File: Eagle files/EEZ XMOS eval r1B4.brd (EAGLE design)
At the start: 100 x 85 mm, 227 parts, among them IC1 TPS61169DCKR, IC10 IS42S16400J, IC11 SN74CBTLV3257, IC12 SN74LVC1G02DBVR, IC13 AT25SF041-SSHDT, IC14 SN74CBTLV3257, IC15 TPS2051BDBVR, IC16 TPD2E001DZDR, IC17 TPS561208DDCR, IC18 XE216-512-TQ128-C20, IC19 TPD4E001DRLR, IC2 TPS561208DDCR, IC20 TPD4E001DRLR, IC21 74LVC1G07SE-7, IC22 74LVC1G07SE-7, IC23 TPA6205A1DGN, IC24 DP83848CVV/NOPB, IC25 M95256-WMN6P, IC26 74VHC595MTC, IC27 PCA21125T/Q900/1,1, IC28 MCP23S17-E/SS, IC3 74VHC595MTC, IC4 TPS561208DDCR, IC5 74VHC595MTC, IC6 TPS3808G33DBVR, IC7 AR1021-I/SS, IC8 TPS3808G09DBVR, IC9 74AUP1G74DC.125, J1 678038020, J2 5033981892, Q1 IRLML2246TRPBF, SW1 1301.9316, X1 FC68149, X2 SSW-105-02-S-D, X3 TSW-104-02-S-D_NN, X4 TSW-103-07-F-D, X5 ZL231-20KG, X6 22-23-2021, X7 LMJTAB881243M-L, X8 SSW-107-02-S-D, X9 PCA-6G-20-HL-3 or 52746-2071, Y1 XTAL016178- 85SMX

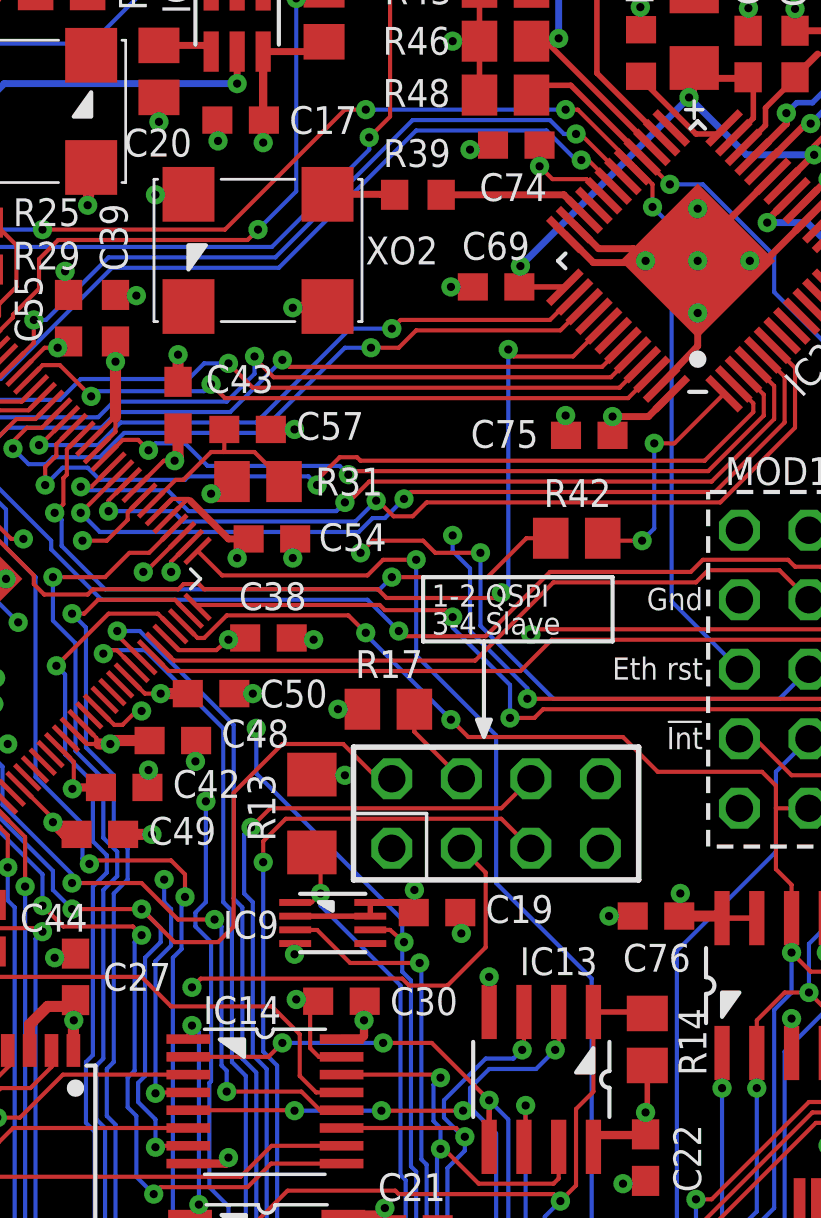
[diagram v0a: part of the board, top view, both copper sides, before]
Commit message: pin swap on X3
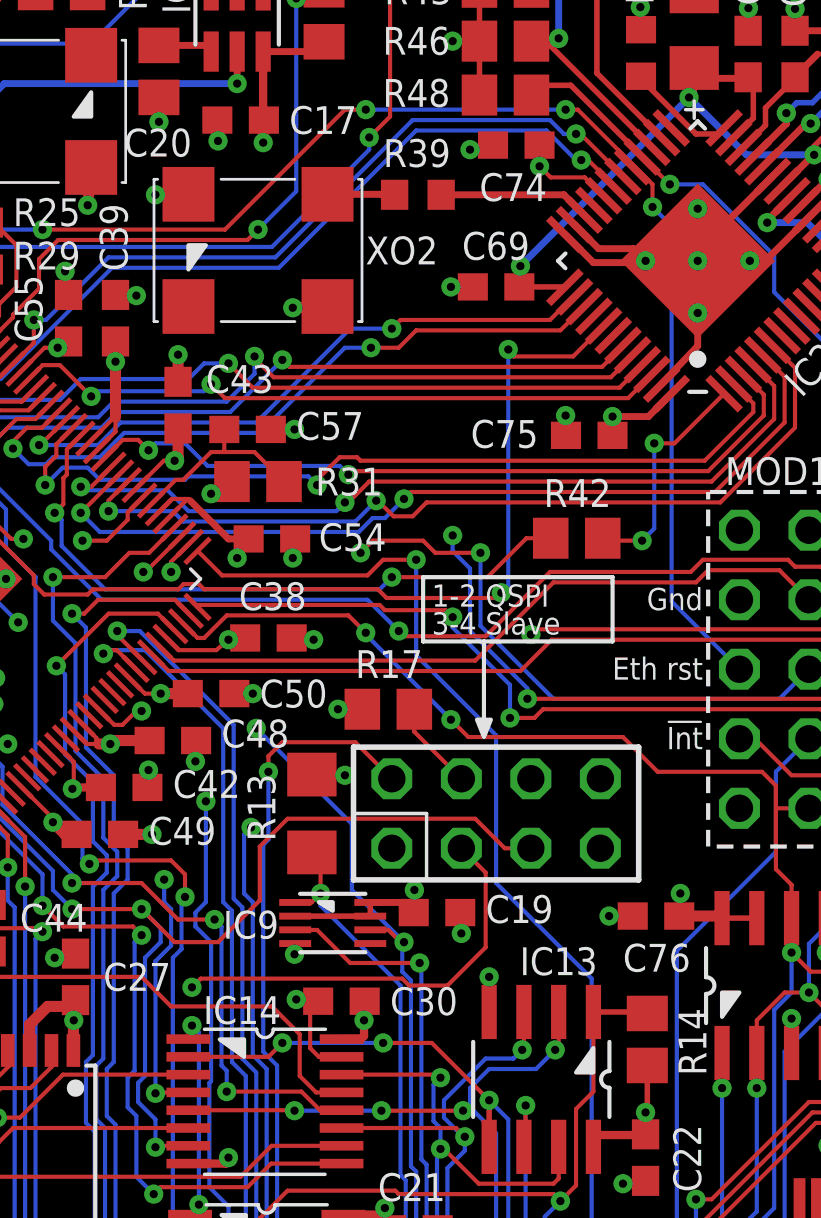
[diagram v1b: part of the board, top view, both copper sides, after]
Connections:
- net LATCH_IN: now also X3.2; no longer X3.5
- net X0D05/QS_D1: now also X3.5; no longer X3.2
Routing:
- net X0D05/QS_D1: track 51.6 -> 53.7 mm
- net LATCH_IN: track 30.9 -> 28.8 mm
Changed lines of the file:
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@@
 <layer number="27" name="tValues" color="12" fill="1" visible="no" active="yes"/>
 <layer number="28" name="bValues" color="11" fill="1" visible="no" active="yes"/>
-<layer number="29" name="tStop" color="7" fill="1" visible="no" active="yes"/>
+<layer number="29" name="tStop" color="7" fill="1" visible="yes" active="yes"/>
 <layer number="30" name="bStop" color="7" fill="1" visible="no" active="yes"/>
 <layer number="31" name="tCream" color="7" fill="4" visible="no" active="yes"/>
@@
 <wire x1="69.4055" y1="71.462" x2="69.4055" y2="72.4154" width="0.254" layer="1"/>
 <wire x1="60.949065625" y1="62.005771875" x2="60.930228125" y2="62.005771875" width="0.2032" layer="1"/>
-<wire x1="60.930228125" y1="62.005771875" x2="60.325" y2="62.611" width="0.1524" layer="1"/>
-<wire x1="60.325" y1="62.611" x2="59.0804" y2="62.611" width="0.1524" layer="1"/>
-<wire x1="59.0804" y1="62.611" x2="58.6105" y2="63.0809" width="0.1524" layer="1"/>
 <wire x1="42.155628125" y1="52.9911" x2="43.076028125" y2="53.9115" width="0.1524" layer="1"/>
 <wire x1="43.1165" y1="55.9435" x2="43.1165" y2="56.681" width="0.4064" layer="1"/>
@@
 <wire x1="29.637284375" y1="53.2765" x2="29.0195" y2="53.2765" width="0.1524" layer="1"/>
 <wire x1="29.0195" y1="53.2765" x2="28.6385" y2="52.8955" width="0.1524" layer="1"/>
+<wire x1="60.930228125" y1="62.005771875" x2="60.2615" y2="62.6745" width="0.1524" layer="1"/>
+<wire x1="60.2615" y1="62.6745" x2="59.0169" y2="62.6745" width="0.1524" layer="1"/>
+<wire x1="59.0169" y1="62.6745" x2="58.6105" y2="63.0809" width="0.1524" layer="1"/>
 </signal>
 <signal name="N$28">
@@
 <wire x1="50.546" y1="12.065" x2="50.8" y2="12.319" width="0.1524" layer="16"/>
 <wire x1="54.102" y1="18.8595" x2="54.102" y2="19.812" width="0.1524" layer="16"/>
-<wire x1="52.4256" y1="35.183" x2="53.1455" y2="35.183" width="0.1524" layer="1"/>
-<wire x1="53.1455" y1="35.183" x2="53.6575" y2="34.7345" width="0.1524" layer="1"/>
 <wire x1="54.102" y1="19.812" x2="54.102" y2="26.3525" width="0.1524" layer="16"/>
 <wire x1="54.102" y1="19.812" x2="54.1655" y2="19.812" width="0.1524" layer="1"/>
@@
 <wire x1="53.9115" y1="33.3375" x2="53.594" y2="33.655" width="0.1524" layer="16"/>
 <wire x1="53.594" y1="33.655" x2="53.594" y2="34.671" width="0.1524" layer="16"/>
-<wire x1="53.594" y1="34.671" x2="53.6575" y2="34.7345" width="0.1524" layer="16"/>
 <wire x1="33.7185" y1="53.5305" x2="24.3205" y2="53.5305" width="0.1524" layer="16"/>
 <wire x1="24.3205" y1="53.5305" x2="23.5585" y2="52.7685" width="0.1524" layer="16"/>
@@
 <wire x1="35.687" y1="50.292" x2="39.5605" y2="46.4185" width="0.1524" layer="16"/>
 <via x="48.26" y="42.545" extent="1-16" drill="0.3" shape="octagon"/>
-<wire x1="48.26" y1="42.545" x2="48.26" y2="40.894" width="0.1524" layer="16"/>
-<wire x1="48.26" y1="40.894" x2="53.594" y2="35.56" width="0.1524" layer="16"/>
-<wire x1="53.594" y1="35.56" x2="53.594" y2="34.798" width="0.1524" layer="16"/>
-<wire x1="53.594" y1="34.798" x2="53.6575" y2="34.7345" width="0.1524" layer="16"/>
 <wire x1="23.495" y1="52.7685" x2="18.669" y2="47.9425" width="0.1524" layer="1"/>
 <wire x1="18.669" y1="47.9425" x2="15.243" y2="47.9425" width="0.1524" layer="1"/>
@@
 <wire x1="39.37" y1="57.559378125" x2="39.369996875" y2="57.559378125" width="0.1524" layer="1"/>
 <wire x1="39.369996875" y1="57.559378125" x2="38.478675" y2="56.66805625" width="0.1524" layer="1"/>
+<wire x1="48.26" y1="42.545" x2="51.7525" y2="39.0525" width="0.1524" layer="16"/>
+<wire x1="51.7525" y1="39.0525" x2="51.7525" y2="36.6395" width="0.1524" layer="16"/>
+<wire x1="53.594" y1="34.671" x2="53.6575" y2="34.7345" width="0.1524" layer="16"/>
+<wire x1="52.4256" y1="35.183" x2="53.082" y2="35.183" width="0.1524" layer="1"/>
+<wire x1="53.6575" y1="34.7345" x2="53.5305" y2="34.7345" width="0.1524" layer="1"/>
+<wire x1="53.5305" y1="34.7345" x2="53.082" y2="35.183" width="0.1524" layer="1"/>
+<wire x1="51.7525" y1="36.6395" x2="53.6575" y2="34.7345" width="0.1524" layer="16"/>
 </signal>
 <signal name="LCD_DE">
@@
 <wire x1="34.4805" y1="43.053" x2="34.7345" y2="43.053" width="0.1524" layer="16"/>
 <wire x1="34.4805" y1="43.053" x2="34.4805" y2="43.2435" width="0.1524" layer="1"/>
-<contactref element="X3" pad="2"/>
-<wire x1="53.213" y1="40.7035" x2="52.705" y2="40.7035" width="0.1524" layer="1"/>
-<wire x1="52.705" y1="40.7035" x2="51.435" y2="41.9735" width="0.1524" layer="1"/>
-<wire x1="51.435" y1="41.9735" x2="49.2125" y2="41.9735" width="0.1524" layer="1"/>
-<wire x1="49.2125" y1="41.9735" x2="47.4345" y2="40.1955" width="0.1524" layer="1"/>
-<wire x1="47.4345" y1="40.1955" x2="47.4345" y2="35.306" width="0.1524" layer="1"/>
-<wire x1="47.4345" y1="35.306" x2="46.863" y2="34.7345" width="0.1524" layer="1"/>
 <wire x1="46.863" y1="34.7345" x2="45.2755" y2="34.7345" width="0.1524" layer="1"/>
 <wire x1="45.2755" y1="34.7345" x2="44.069" y2="35.941" width="0.1524" layer="1"/>
 <wire x1="26.9875" y1="47.4345" x2="26.9875" y2="47.5615" width="0.1524" layer="1"/>
 <wire x1="27.813" y1="48.387" x2="26.9875" y2="47.5615" width="0.1524" layer="1"/>
+<contactref element="X3" pad="5"/>
+<wire x1="58.293" y1="38.1635" x2="57.3405" y2="38.1635" width="0.1524" layer="1"/>
+<wire x1="57.3405" y1="38.1635" x2="56.261" y2="39.243" width="0.1524" layer="1"/>
+<wire x1="56.261" y1="39.243" x2="49.403" y2="39.243" width="0.1524" layer="1"/>
+<wire x1="49.403" y1="39.243" x2="48.387" y2="38.227" width="0.1524" layer="1"/>
+<wire x1="48.387" y1="38.227" x2="48.387" y2="36.2585" width="0.1524" layer="1"/>
+<wire x1="48.387" y1="36.2585" x2="46.863" y2="34.7345" width="0.1524" layer="1"/>
 </signal>
 <signal name="X0D06/QS_D2">
@@
 <wire x1="46.482" y1="38.862" x2="48.006" y2="38.862" width="0.1524" layer="15"/>
 <wire x1="48.006" y1="38.862" x2="48.0695" y2="38.9255" width="0.1524" layer="15"/>
-<wire x1="57.2135" y1="39.624" x2="48.768" y2="39.624" width="0.1524" layer="1"/>
-<wire x1="48.768" y1="39.624" x2="48.0695" y2="38.9255" width="0.1524" layer="1"/>
+<wire x1="57.2135" y1="39.624" x2="48.768" y2="39.624" width="0.1524" layer="15"/>
+<wire x1="48.768" y1="39.624" x2="48.0695" y2="38.9255" width="0.1524" layer="15"/>
 <contactref element="X3" pad="6"/>
-<wire x1="57.2135" y1="39.624" x2="58.293" y2="40.7035" width="0.1524" layer="1"/>
+<wire x1="57.2135" y1="39.624" x2="58.293" y2="40.7035" width="0.1524" layer="15"/>
 </signal>
 <signal name="N$31">
@@
 </signal>
 <signal name="LATCH_IN">
-<contactref element="X3" pad="5"/>
 <via x="49.911" y="20.193" extent="1-16" drill="0.3" shape="octagon"/>
 <wire x1="49.911" y1="20.193" x2="49.911" y2="21.463" width="0.1524" layer="16"/>
@@
 <wire x1="49.022" y1="22.352" x2="49.022" y2="30.226" width="0.1524" layer="16"/>
 <wire x1="49.022" y1="30.226" x2="48.514" y2="30.734" width="0.1524" layer="16"/>
-<wire x1="48.514" y1="30.734" x2="48.514" y2="37.6555" width="0.1524" layer="16"/>
-<via x="48.514" y="37.6555" extent="1-16" drill="0.3" shape="octagon"/>
-<wire x1="48.514" y1="37.6555" x2="48.514" y2="38.4175" width="0.1524" layer="1"/>
+<via x="48.7045" y="40.9575" extent="1-16" drill="0.3" shape="octagon"/>
 <contactref element="IC11" pad="9"/>
 <wire x1="51.441" y1="20.229" x2="49.947" y2="20.229" width="0.1524" layer="1"/>
 <wire x1="49.947" y1="20.229" x2="49.911" y2="20.193" width="0.1524" layer="1"/>
-<wire x1="49.3395" y1="39.243" x2="48.514" y2="38.4175" width="0.1524" layer="1"/>
-<wire x1="49.3395" y1="39.243" x2="57.2135" y2="39.243" width="0.1524" layer="1"/>
-<wire x1="57.2135" y1="39.243" x2="58.293" y2="38.1635" width="0.1524" layer="1"/>
+<contactref element="X3" pad="2"/>
+<wire x1="48.514" y1="30.734" x2="48.514" y2="38.2905" width="0.1524" layer="16"/>
+<wire x1="48.514" y1="38.2905" x2="48.7045" y2="38.481" width="0.1524" layer="16"/>
+<wire x1="48.7045" y1="38.481" x2="48.7045" y2="40.9575" width="0.1524" layer="16"/>
+<wire x1="53.213" y1="40.7035" x2="51.8795" y2="42.037" width="0.1524" layer="1"/>
+<wire x1="51.8795" y1="42.037" x2="49.2125" y2="42.037" width="0.1524" layer="1"/>
+<wire x1="49.2125" y1="42.037" x2="48.7045" y2="41.529" width="0.1524" layer="1"/>
+<wire x1="48.7045" y1="40.9575" x2="48.7045" y2="41.529" width="0.1524" layer="1"/>
 </signal>
 <signal name="N$14">
@@
 </signal>
 </signals>
+<errors>
+</errors>
 </board>
 </drawing>
